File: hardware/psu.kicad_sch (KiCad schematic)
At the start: 59 parts, among them IC301 TLV61220DBVT, J301 Barrel_Jack_Switch, J302 Conn_01x03, Q301 CSD87503Q3E, Q302 CSD87503Q3E, Q303 Q_NMOS, U301 TPS63020DSJR, U302 BQ25798RQMR

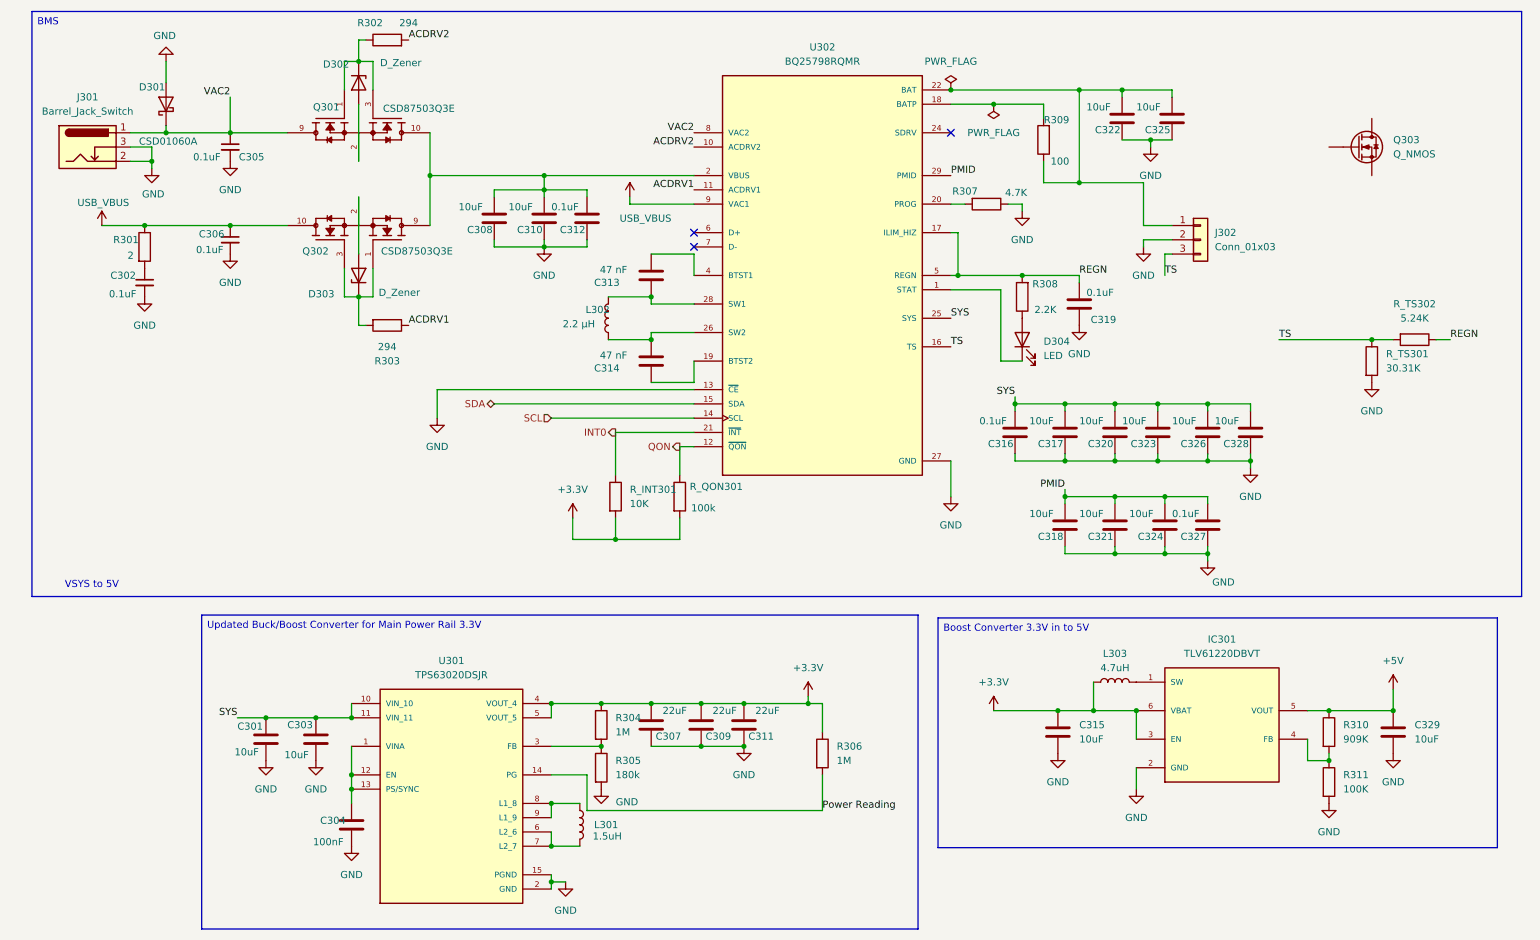
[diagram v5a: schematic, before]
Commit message: added ship fet
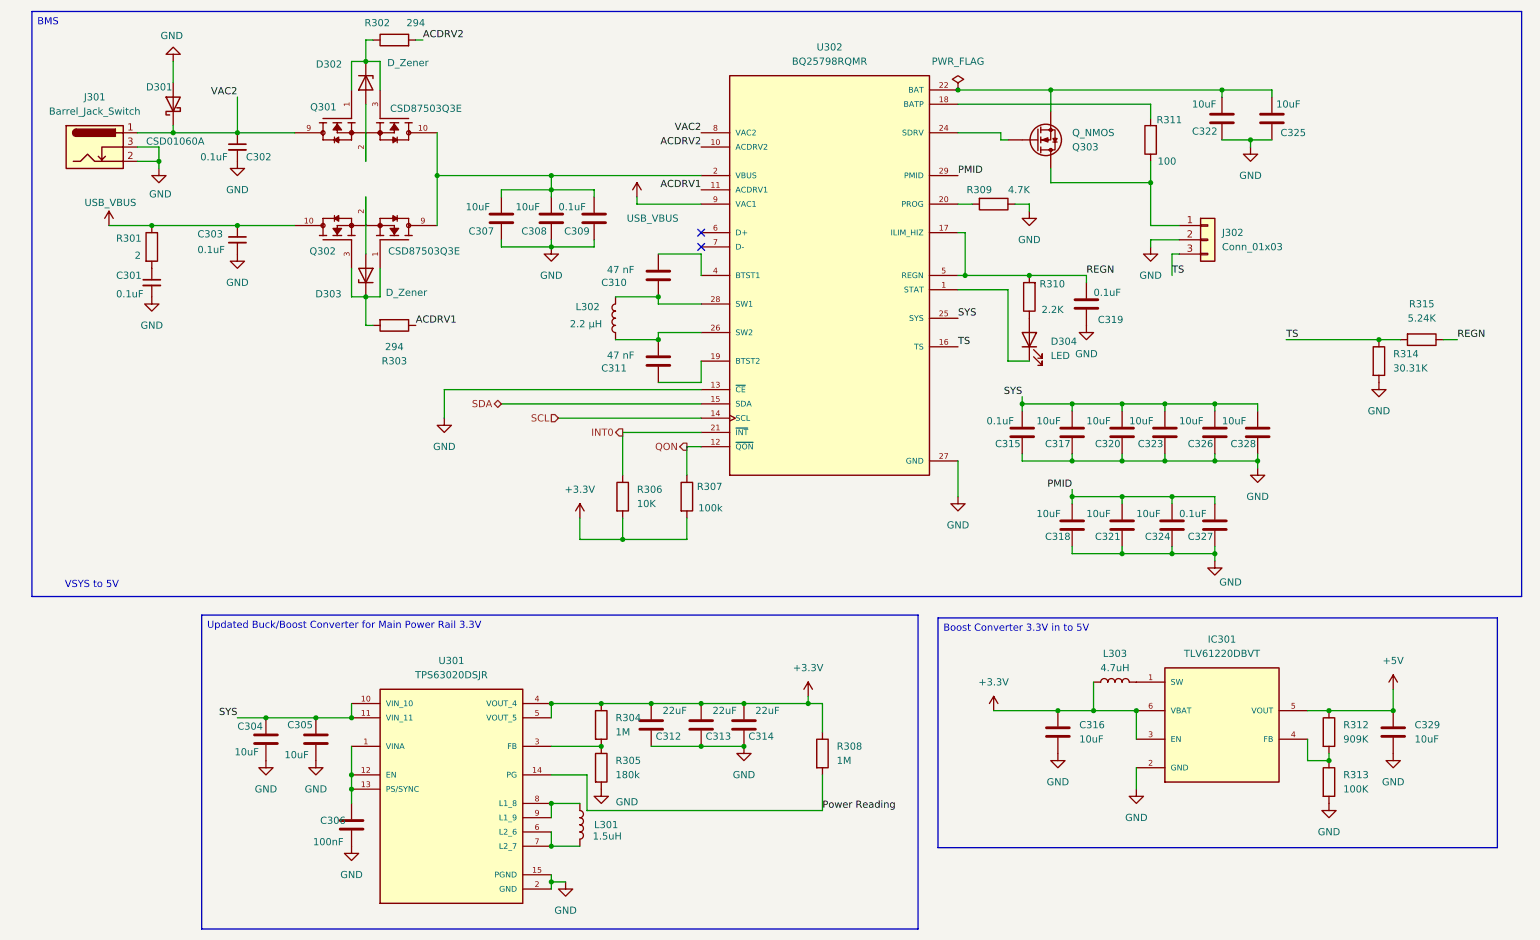
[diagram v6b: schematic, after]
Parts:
- renumbered C302 to C301, C305 to C302, C306 to C303, C301 to C304, C303 to C305, C304 to C306, C308 to C307, C310 to C308, C312 to C309, C313 to C310, C314 to C311, C307 to C312, C309 to C313, C311 to C314, C316 to C315, C315 to C316, R_INT301 to R306, R_QON301 to R307, R306 to R308, R307 to R309, R308 to R310, R309 to R311, R310 to R312, R311 to R313, R_TS301 to R314, R_TS302 to R315
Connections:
- net BAT: now also Q303.S; no longer J302.1 (Pin_1), R311.1
- net at Q303.D: now also J302.1 (Pin_1), R311.1
- net at Q303.G: now also U302.24 (SDRV)
- no-connect marks 3 -> 2
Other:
- moved on the sheet: C301, C302, C303, C307, C308, C309, C310, C311, C315, C317, C318, C319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

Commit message: footprint update
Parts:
- C301, C302, C303, C307, C308, C309, C310, C311, C315, C317, C318, C319, C320, C321, C322, C323, C324, C325, C326, C327, C328: footprint Capacitor_SMD:C_0402_1005Metric -> Capacitor_SMD:C_0805_2012Metric
- C304, C305, C306, C312, C313, C314, C316, C329: footprint (none) -> Capacitor_SMD:C_0805_2012Metric
- L301, L303: footprint (none) -> Inductor_SMD:L_0805_2012Metric
- L302: footprint Inductor_SMD:L_7.3x7.3_H3.5 -> Inductor_SMD:L_0805_2012Metric
- R304, R305, R308, R312, R313: footprint (none) -> Resistor_SMD:R_0805_2012Metric
- U301: footprint TPS63020DSJR:IC_TPS63020DSJR -> pyronet_footprints:IC_TPS63020DSJR
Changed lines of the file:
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@@
 			)
 		)
-		(property "Footprint" ""
+		(property "Footprint" "Capacitor_SMD:C_0805_2012Metric"
 			(at 124.7648 137.16 0)
 			(effects
@@
 			)
 		)
-		(property "Footprint" "Capacitor_SMD:C_0402_1005Metric"
+		(property "Footprint" "Capacitor_SMD:C_0805_2012Metric"
 			(at 226.3648 36.83 0)
 			(effects
@@
 			)
 		)
-		(property "Footprint" "Capacitor_SMD:C_0402_1005Metric"
+		(property "Footprint" "Capacitor_SMD:C_0805_2012Metric"
 			(at 52.07 38.1 0)
 			(effects
@@
 			)
 		)
-		(property "Footprint" "Capacitor_SMD:C_0402_1005Metric"
+		(property "Footprint" "Capacitor_SMD:C_0805_2012Metric"
 			(at 36.83 62.23 0)
 			(effects
@@
 			)
 		)
-		(property "Footprint" "Capacitor_SMD:C_0402_1005Metric"
+		(property "Footprint" "Capacitor_SMD:C_0805_2012Metric"
 			(at 225.0948 92.71 0)
 			(effects
@@
 			)
 		)
-		(property "Footprint" "Capacitor_SMD:C_0402_1005Metric"
+		(property "Footprint" "Capacitor_SMD:C_0805_2012Metric"
 			(at 216.2048 92.71 0)
 			(effects
@@
 			)
 		)
-		(property "Footprint" ""
+		(property "Footprint" "Resistor_SMD:R_0805_2012Metric"
 			(at 115.062 140.97 90)
 			(effects
@@
 			)
 		)
-		(property "Footprint" ""
+		(property "Footprint" "Resistor_SMD:R_0805_2012Metric"
 			(at 244.602 151.13 90)
 			(effects
@@
 			)
 		)
-		(property "Footprint" ""
+		(property "Footprint" "Capacitor_SMD:C_0805_2012Metric"
 			(at 58.1152 147.32 0)
 			(effects
@@
 			)
 		)
-		(property "Footprint" "Capacitor_SMD:C_0402_1005Metric"
+		(property "Footprint" "Capacitor_SMD:C_0805_2012Metric"
 			(at 98.0948 54.61 0)
 			(effects
@@
 			)
 		)
-		(property "Footprint" "Capacitor_SMD:C_0402_1005Metric"
+		(property "Footprint" "Capacitor_SMD:C_0805_2012Metric"
 			(at 106.9848 54.61 0)
 			(effects
@@
 			)
 		)
-		(property "Footprint" ""
+		(property "Footprint" "Capacitor_SMD:C_0805_2012Metric"
 			(at 258.7752 146.05 0)
 			(effects
@@
 			)
 		)
-		(property "Footprint" "Capacitor_SMD:C_0402_1005Metric"
+		(property "Footprint" "Capacitor_SMD:C_0805_2012Metric"
 			(at 208.5848 92.71 0)
 			(effects
@@
 			)
 		)
-		(property "Footprint" "Capacitor_SMD:C_0402_1005Metric"
+		(property "Footprint" "Capacitor_SMD:C_0805_2012Metric"
 			(at 235.2548 36.83 0)
 			(effects
@@
 			)
 		)
-		(property "Footprint" ""
+		(property "Footprint" "Capacitor_SMD:C_0805_2012Metric"
 			(at 73.3552 162.56 0)
 			(effects
@@
 			)
 		)
-		(property "Footprint" ""
+		(property "Footprint" "Resistor_SMD:R_0805_2012Metric"
 			(at 115.062 148.59 90)
 			(effects
@@
 			)
 		)
-		(property "Footprint" ""
+		(property "Footprint" "Inductor_SMD:L_0805_2012Metric"
 			(at 208.28 133.35 0)
 			(effects
@@
 			)
 		)
-		(property "Footprint" ""
+		(property "Footprint" "Resistor_SMD:R_0805_2012Metric"
 			(at 154.432 146.05 90)
 			(effects
@@
 			)
 		)
-		(property "Footprint" "Capacitor_SMD:C_0402_1005Metric"
+		(property "Footprint" "Capacitor_SMD:C_0805_2012Metric"
 			(at 126.0348 80.01 0)
 			(effects
@@
 			)
 		)
-		(property "Footprint" "Capacitor_SMD:C_0402_1005Metric"
+		(property "Footprint" "Capacitor_SMD:C_0805_2012Metric"
 			(at 126.0348 64.77 0)
 			(effects
@@
 			)
 		)
-		(property "Footprint" "Capacitor_SMD:C_0402_1005Metric"
+		(property "Footprint" "Capacitor_SMD:C_0805_2012Metric"
 			(at 217.4748 109.22 0)
 			(effects
@@
 			)
 		)
-		(property "Footprint" "Capacitor_SMD:C_0402_1005Metric"
+		(property "Footprint" "Capacitor_SMD:C_0805_2012Metric"
 			(at 225.0948 109.22 0)
 			(effects
@@
 			)
 		)
-		(property "Footprint" "Capacitor_SMD:C_0402_1005Metric"
+		(property "Footprint" "Capacitor_SMD:C_0805_2012Metric"
 			(at 114.6048 54.61 0)
 			(effects
@@
 			)
 		)
-		(property "Footprint" ""
+		(property "Footprint" "Capacitor_SMD:C_0805_2012Metric"
 			(at 67.0052 147.32 0)
 			(effects
@@
 			)
 		)
-		(property "Footprint" "Capacitor_SMD:C_0402_1005Metric"
+		(property "Footprint" "Capacitor_SMD:C_0805_2012Metric"
 			(at 199.6948 92.71 0)
 			(effects
@@
 			)
 		)
-		(property "Footprint" "Capacitor_SMD:C_0402_1005Metric"
+		(property "Footprint" "Capacitor_SMD:C_0805_2012Metric"
 			(at 202.2348 69.85 0)
 			(effects
@@
 			)
 		)
-		(property "Footprint" "Capacitor_SMD:C_0402_1005Metric"
+		(property "Footprint" "Capacitor_SMD:C_0805_2012Metric"
 			(at 208.5848 109.22 0)
 			(effects
@@
 			)
 		)
-		(property "Footprint" "Inductor_SMD:L_7.3x7.3_H3.5"
+		(property "Footprint" "Inductor_SMD:L_0805_2012Metric"
 			(at 119.38 68.58 0)
 			(effects
@@
 			)
 		)
-		(property "Footprint" ""
+		(property "Footprint" "Inductor_SMD:L_0805_2012Metric"
 			(at 113.03 158.75 0)
 			(effects
@@
 			)
 		)
-		(property "Footprint" "Capacitor_SMD:C_0402_1005Metric"
+		(property "Footprint" "Capacitor_SMD:C_0805_2012Metric"
 			(at 199.6948 109.22 0)
 			(effects
@@
 			)
 		)
-		(property "Footprint" "TPS63020DSJR:IC_TPS63020DSJR"
+		(property "Footprint" "pyronet_footprints:IC_TPS63020DSJR"
 			(at 90.17 152.4 0)
 			(effects
@@
 			)
 		)
-		(property "Footprint" "Capacitor_SMD:C_0402_1005Metric"
+		(property "Footprint" "Capacitor_SMD:C_0805_2012Metric"
 			(at 232.7148 92.71 0)
 			(effects
@@
 			)
 		)
-		(property "Footprint" ""
+		(property "Footprint" "Resistor_SMD:R_0805_2012Metric"
 			(at 244.602 142.24 90)
 			(effects
@@
 			)
 		)
-		(property "Footprint" ""
+		(property "Footprint" "Capacitor_SMD:C_0805_2012Metric"
 			(at 199.0852 146.05 0)
 			(effects
@@
 			)
 		)
-		(property "Footprint" ""
+		(property "Footprint" "Capacitor_SMD:C_0805_2012Metric"
 			(at 141.2748 137.16 0)
 			(effects
@@
 			)
 		)
-		(property "Footprint" ""
+		(property "Footprint" "Capacitor_SMD:C_0805_2012Metric"
 			(at 133.6548 137.16 0)
 			(effects
@@
 			)
 		)
-		(property "Footprint" "Capacitor_SMD:C_0402_1005Metric"
+		(property "Footprint" "Capacitor_SMD:C_0805_2012Metric"
 			(at 190.8048 92.71 0)
 			(effects
@@
 			)
 		)
-		(property "Footprint" "Capacitor_SMD:C_0402_1005Metric"
+		(property "Footprint" "Capacitor_SMD:C_0805_2012Metric"
 			(at 52.07 54.61 0)
 			(effects

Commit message: footprint update 2
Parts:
- D301: footprint Package_TO_SOT_THT:TO-220-2_Vertical -> Diode_SMD:D_SOD-123
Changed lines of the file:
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@@
 			)
 		)
-		(property "Footprint" "Package_TO_SOT_THT:TO-220-2_Vertical"
+		(property "Footprint" "Diode_SMD:D_SOD-123"
 			(at 45.085 30.48 0)
 			(effects
